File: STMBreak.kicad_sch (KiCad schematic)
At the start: 12 parts, among them J1 Conn_01x04_Pin, J2 USB_C_Receptacle_USB2.0_14P, U1 AMS1117-3.3, U2 AS5600, U3 STM32F103C8Tx, Y1 8M

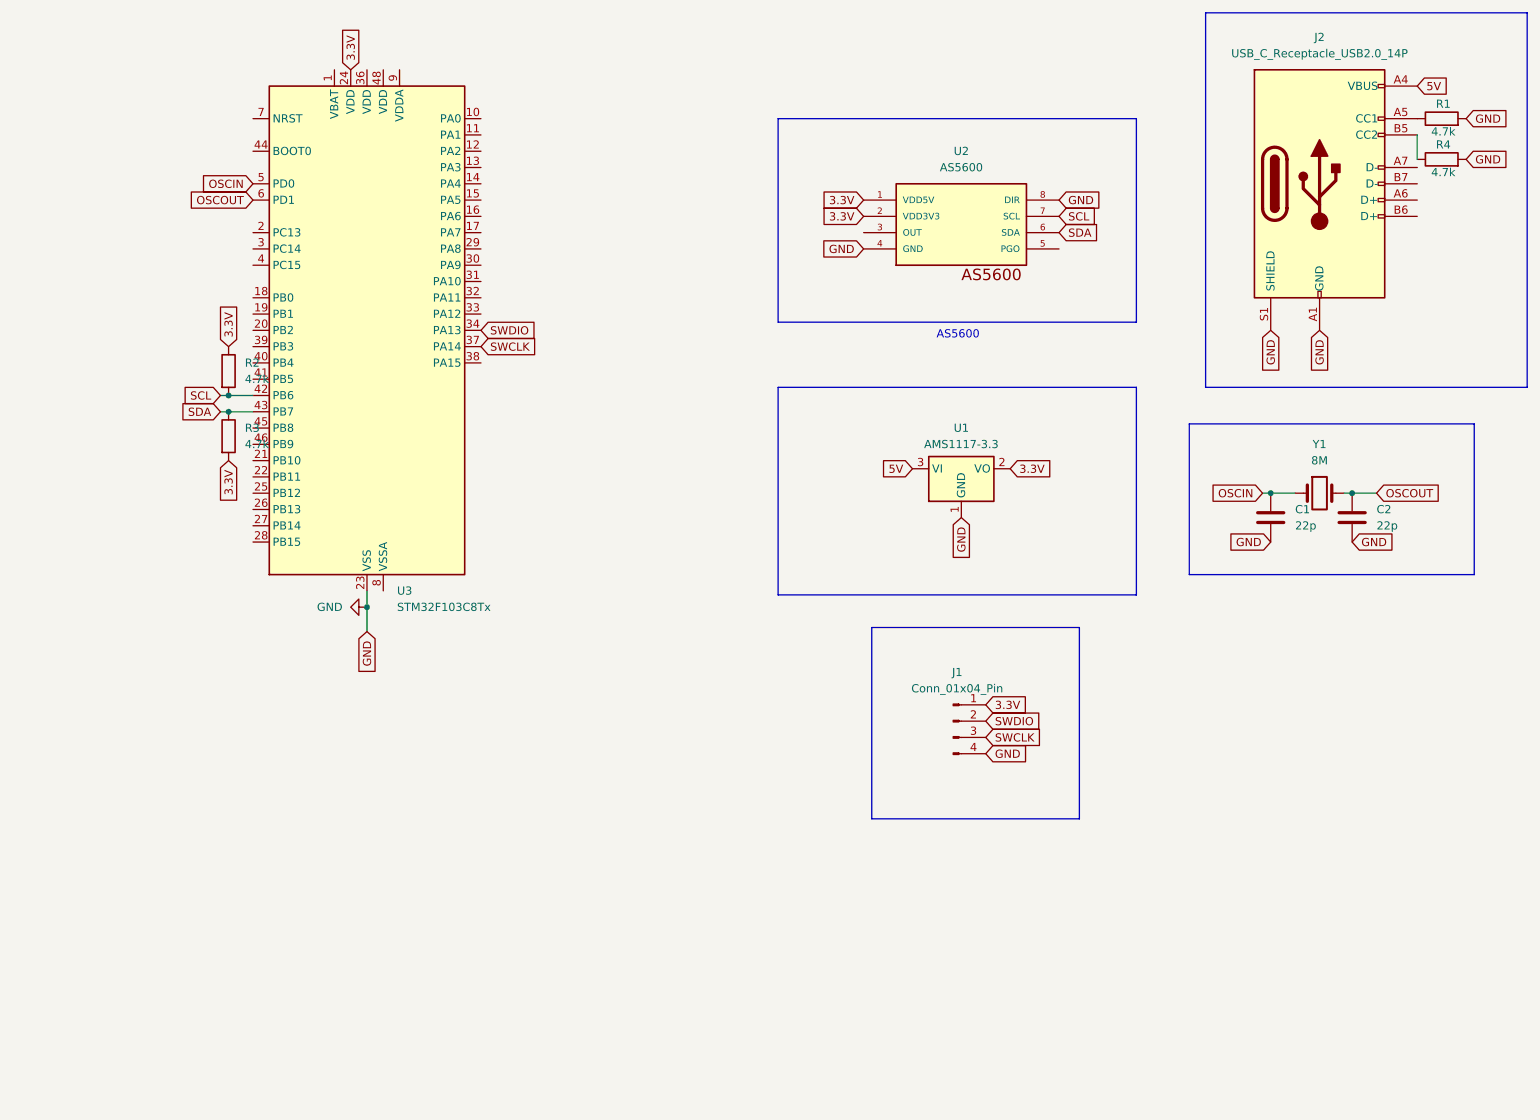
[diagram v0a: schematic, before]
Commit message: Add files via upload
Capacitors, ferrite beads and other components added. Traces modified. Ground plane added.
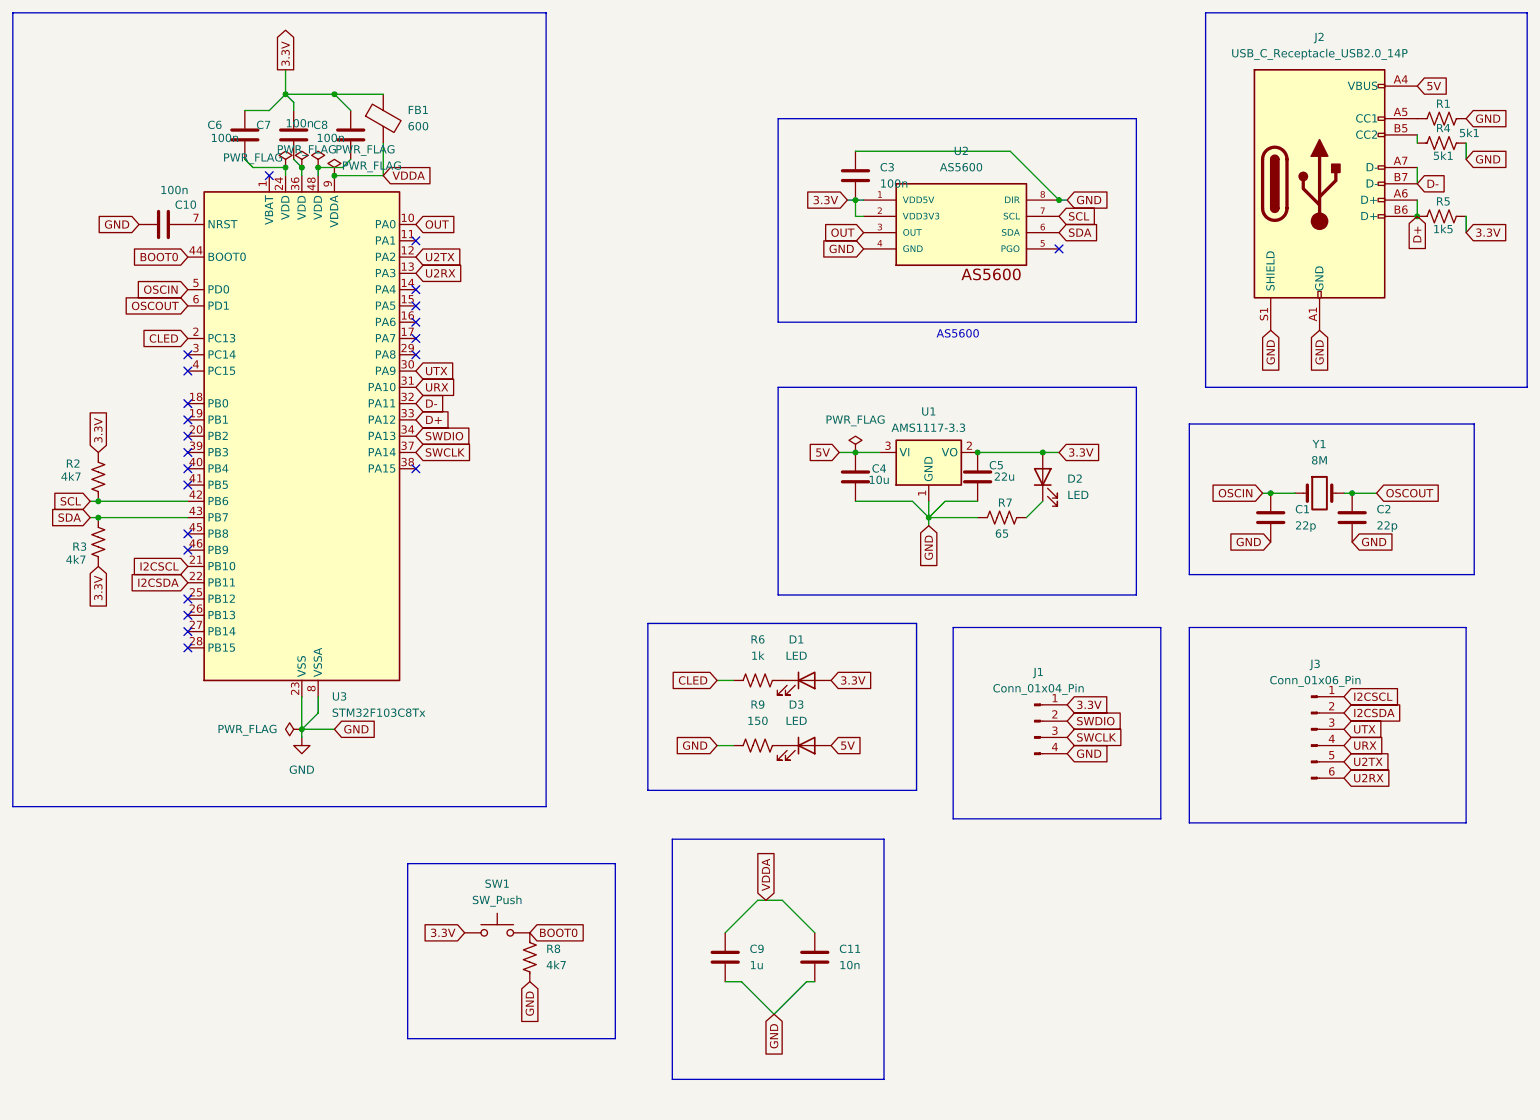
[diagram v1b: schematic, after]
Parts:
- added C10, C3, C6, C7, C8: 100n, Capacitor_SMD:C_0603_1608Metric_Pad1.08x0.95mm_HandSolder, symbol Device:C
- added C11: 10n, Capacitor_SMD:C_0603_1608Metric_Pad1.08x0.95mm_HandSolder, symbol Device:C
- added C4: 10u, Capacitor_SMD:C_0603_1608Metric_Pad1.08x0.95mm_HandSolder, symbol Device:C
- added C5: 22u, Capacitor_SMD:C_0603_1608Metric_Pad1.08x0.95mm_HandSolder, symbol Device:C
- added C9: 1u, Capacitor_SMD:C_0603_1608Metric_Pad1.08x0.95mm_HandSolder, symbol Device:C
- added D1, D2, D3: LED, LED_SMD:LED_0603_1608Metric_Pad1.05x0.95mm_HandSolder, symbol Device:LED
- added FB1: 600, FerriteBead:FB_LI0603G121R-10, symbol Device:FerriteBead
- added J3: Conn_01x06_Pin, Connector_PinSocket_2.54mm:PinSocket_1x06_P2.54mm_Vertical, symbol Connector:Conn_01x06_Pin
- added R5: 1k5, Resistor_SMD:R_0603_1608Metric_Pad0.98x0.95mm_HandSolder, symbol Device:R_US
- added R6: 1k, Resistor_SMD:R_0603_1608Metric_Pad0.98x0.95mm_HandSolder, symbol Device:R_US
- added R7: 65, Resistor_SMD:R_0603_1608Metric_Pad0.98x0.95mm_HandSolder, symbol Device:R_US
- added R8: 4k7, Resistor_SMD:R_0603_1608Metric_Pad0.98x0.95mm_HandSolder, symbol Device:R_US
- added R9: 150, Resistor_SMD:R_0603_1608Metric_Pad0.98x0.95mm_HandSolder, symbol Device:R_US
- added SW1: SW_Push, Button_Switch_SMD:Panasonic_EVQPUJ_EVQPUA, symbol Switch:SW_Push
- C2: footprint Capacitor_SMD:C_0805_2012Metric_Pad1.18x1.45mm_HandSolder -> Capacitor_SMD:C_0603_1608Metric_Pad1.08x0.95mm_HandSolder
- J2: footprint Connector_USB:USB_C_Receptacle_G-Switch_GT-USB-7051x -> Connector_USB:USB_C_Receptacle_GCT_USB4105-xx-A_16P_TopMnt_Horizontal
- R1, R4: value 4.7k -> 5k1; symbol Device:R -> Device:R_US
- R2, R3: value 4.7k -> 4k7; symbol Device:R -> Device:R_US
- Y1: footprint Crystal:Crystal_C26-LF_D2.1mm_L6.5mm_Horizontal -> Crystal:Crystal_HC49-U_Horizontal
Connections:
- net 3.3V: now also C3.2, C5.1, C6.1, C7.1, C8.1, D1.2 (A), D2.2 (A), FB1.1, R5.2, SW1.1; no longer U3.24 (VDD)
- net 5V: now also C4.1, D3.2 (A)
- net GND: now also U3.8 (VSSA), C10.2, C11.2, C3.1, C4.2, C5.2, C9.2, R7.1, R8.1, R9.1
- net OUT: now reaches U3.10 (PA0)
- net OUT: now also U2.3 (OUT)
- net U2TX: now reaches U3.12 (PA2)
- net U2TX: now also J3.5 (Pin_5)
- net U2RX: now reaches U3.13 (PA3)
- net U2RX: now also J3.6 (Pin_6)
- net CLED: now reaches U3.2 (PC13)
- net CLED: now also R6.1
- net I2CSCL: now reaches U3.21 (PB10)
- net I2CSCL: now also J3.1 (Pin_1)
- net I2CSDA: now reaches U3.22 (PB11)
- net I2CSDA: now also J3.2 (Pin_2)
- net UTX: now reaches U3.30 (PA9)
- net UTX: now also J3.3 (Pin_3)
- net URX: now reaches U3.31 (PA10)
- net URX: now also J3.4 (Pin_4)
- net D-: now reaches U3.32 (PA11)
- net D-: now also J2.A7 (D-), J2.B7 (D-)
- net D+: now reaches U3.33 (PA12)
- net D+: now also J2.A6 (D+), J2.B6 (D+), R5.1
- net at U3.36 (VDD): now also C7.2
- net BOOT0: now reaches U3.44 (BOOT0)
- net BOOT0: now also R8.2, SW1.2
- net at U3.48 (VDD): now also C8.2
- net at U3.7 (NRST): now also C10.1
- net VDDA: now reaches U3.9 (VDDA)
- net VDDA: now also C11.1, C9.1, FB1.2
- new net: C6.2, U3.24 (VDD)
- new net: D1.1 (K), R6.2
- new net: D3.1 (K), R9.2
- new net: D2.1 (K), R7.2
- no-connect marks 0 -> 23
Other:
- moved on the sheet: J1, U1, U3

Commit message: Add files via upload
Centered AS5600.
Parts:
- Y1: footprint Crystal:Crystal_HC49-U_Horizontal -> Crystal:Crystal_SMD_HC49-SD_HandSoldering
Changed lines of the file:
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@@
 			)
 		)
-		(property "Footprint" "Crystal:Crystal_HC49-U_Horizontal"
+		(property "Footprint" "Crystal:Crystal_SMD_HC49-SD_HandSoldering"
 			(at 224.79 96.52 0)
 			(effects

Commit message: Add files via upload
Modified design approach.
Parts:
- SW1: footprint Button_Switch_SMD:Panasonic_EVQPUJ_EVQPUA -> TS09:SW_TS09-63-25-R-260-SMT-TR
- Y1: footprint Crystal:Crystal_SMD_HC49-SD_HandSoldering -> Crystal:Crystal_SMD_Abracon_ABM3-2Pin_5.0x3.2mm_HandSoldering
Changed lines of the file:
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@@
 			)
 		)
-		(property "Footprint" "Button_Switch_SMD:Panasonic_EVQPUJ_EVQPUA"
+		(property "Footprint" "TS09:SW_TS09-63-25-R-260-SMT-TR"
 			(at 96.52 160.02 0)
 			(effects
@@
 			)
 		)
-		(property "Footprint" "Crystal:Crystal_SMD_HC49-SD_HandSoldering"
+		(property "Footprint" "Crystal:Crystal_SMD_Abracon_ABM3-2Pin_5.0x3.2mm_HandSoldering"
 			(at 224.79 96.52 0)
 			(effects

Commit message: Add files via upload
Updated trace design.
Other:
- note added: "CRYSTAL"
- note added: "DUMMY PINS"
- note added: "LDO"
- note added: "LEDs"
- note added: "RESET BUTTON"
- note added: "STM32F103C8T6"
- note added: "SWD"
- note added: "USB C"
- note added: "VDDA CAPS"
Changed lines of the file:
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@@
+		)
+	)
+	(text "VDDA CAPS\n"
+		(exclude_from_sim no)
+		(at 140.716 191.262 0)
+		(effects
+			(font
+				(size 1.27 1.27)
+			)
+		)
+	)
+	(text "STM32F103C8T6"
+		(exclude_from_sim no)
+		(at 60.706 149.352 0)
+		(effects
+			(font
+				(size 1.27 1.27)
+			)
+		)
+	)
+	(text "LEDs\n"
+		(exclude_from_sim no)
+		(at 140.462 145.288 0)
+		(effects
+			(font
+				(size 1.27 1.27)
+			)
+		)
+	)
+	(text "DUMMY PINS\n"
+		(exclude_from_sim no)
+		(at 225.298 150.368 0)
+		(effects
+			(font
+				(size 1.27 1.27)
+			)
+		)
+	)
+	(text "CRYSTAL\n"
+		(exclude_from_sim no)
+		(at 227.33 111.506 0)
+		(effects
+			(font
+				(size 1.27 1.27)
+			)
+		)
+	)
+	(text "LDO\n"
+		(exclude_from_sim no)
+		(at 167.386 114.046 0)
+		(effects
+			(font
+				(size 1.27 1.27)
+			)
 		)
 	)
@@
 		(effects
 			(font
+				(size 1.27 1.27)
+			)
+		)
+	)
+	(text "RESET BUTTON"
+		(exclude_from_sim no)
+		(at 97.282 185.42 0)
+		(effects
+			(font
+				(size 1.27 1.27)
+			)
+		)
+	)
+	(text "USB C\n"
+		(exclude_from_sim no)
+		(at 230.124 82.804 0)
+		(effects
+			(font
+				(size 1.27 1.27)
+			)
+		)
+	)
+	(text "SWD\n"
+		(exclude_from_sim no)
+		(at 183.388 150.368 0)
+		(effects
+			(font

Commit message: Add files via upload
Modified PCB design.
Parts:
- C1, C2: value 22p -> 30p
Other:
- note added: "CRYSTAL 8Mhz"
- note removed: "CRYSTAL"
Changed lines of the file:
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@@
 		)
 	)
-	(text "CRYSTAL\n"
+	(text "CRYSTAL 8Mhz\n"
 		(exclude_from_sim no)
 		(at 227.33 111.506 0)
@@
 			)
 		)
-		(property "Value" "22p"
+		(property "Value" "30p"
 			(at 220.98 101.5999 0)
 			(effects
@@
 			)
 		)
-		(property "Value" "22p"
+		(property "Value" "30p"
 			(at 233.68 101.5999 0)
 			(effects
